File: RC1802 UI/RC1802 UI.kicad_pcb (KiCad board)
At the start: 2 copper layers, 99.1 x 80 mm, 44 parts, among them J1 Mount, J2 Mount, J3 Mount, J4 Mount, J6 CONN_02X20, SW1 CLEAR, SW10 IN5, SW11 IN6, SW12 IN7, SW2 IN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

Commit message: Tied leftover LS04 and 4050 inputs low
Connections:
- U1 pad 13: (no net) -> GND
- U2 pad 11: (no net) -> GND
- U2 pad 14: (no net) -> GND
- U2 pad 7: (no net) -> GND
- U2 pad 9: (no net) -> GND
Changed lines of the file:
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@@
 (kicad_pcb (version 4) (host pcbnew 4.0.7)
   (general
-    (links 160)
+    (links 165)
     (no_connects 0)
     (area 100.254999 67.234999 199.465001 147.395001)
@@
     (pad 1 thru_hole rect (at 0 0) (size 1.6 1.6) (drill 0.8) (layers *.Cu *.Mask)
       (net 16 VCC))
-    (pad 9 thru_hole oval (at 7.62 17.78) (size 1.6 1.6) (drill 0.8) (layers *.Cu *.Mask))
+    (pad 9 thru_hole oval (at 7.62 17.78) (size 1.6 1.6) (drill 0.8) (layers *.Cu *.Mask)
+      (net 3 GND))
     (pad 2 thru_hole oval (at 0 2.54) (size 1.6 1.6) (drill 0.8) (layers *.Cu *.Mask)
       (net 60 ~CLEAR))
@@
     (pad 3 thru_hole oval (at 0 5.08) (size 1.6 1.6) (drill 0.8) (layers *.Cu *.Mask)
       (net 60 ~CLEAR))
-    (pad 11 thru_hole oval (at 7.62 12.7) (size 1.6 1.6) (drill 0.8) (layers *.Cu *.Mask))
+    (pad 11 thru_hole oval (at 7.62 12.7) (size 1.6 1.6) (drill 0.8) (layers *.Cu *.Mask)
+      (net 3 GND))
     (pad 4 thru_hole oval (at 0 7.62) (size 1.6 1.6) (drill 0.8) (layers *.Cu *.Mask)
       (net 48 STROBE))
@@
     (pad 13 thru_hole oval (at 7.62 7.62) (size 1.6 1.6) (drill 0.8) (layers *.Cu *.Mask))
     (pad 6 thru_hole oval (at 0 12.7) (size 1.6 1.6) (drill 0.8) (layers *.Cu *.Mask))
-    (pad 14 thru_hole oval (at 7.62 5.08) (size 1.6 1.6) (drill 0.8) (layers *.Cu *.Mask))
-    (pad 7 thru_hole oval (at 0 15.24) (size 1.6 1.6) (drill 0.8) (layers *.Cu *.Mask))
+    (pad 14 thru_hole oval (at 7.62 5.08) (size 1.6 1.6) (drill 0.8) (layers *.Cu *.Mask)
+      (net 3 GND))
+    (pad 7 thru_hole oval (at 0 15.24) (size 1.6 1.6) (drill 0.8) (layers *.Cu *.Mask)
+      (net 3 GND))
     (pad 15 thru_hole oval (at 7.62 2.54) (size 1.6 1.6) (drill 0.8) (layers *.Cu *.Mask))
     (pad 8 thru_hole oval (at 0 17.78) (size 1.6 1.6) (drill 0.8) (layers *.Cu *.Mask)
@@
     (pad 6 thru_hole oval (at 0 12.7) (size 1.6 1.6) (drill 0.8) (layers *.Cu *.Mask)
       (net 59 ~WAIT))
-    (pad 13 thru_hole oval (at 7.62 2.54) (size 1.6 1.6) (drill 0.8) (layers *.Cu *.Mask))
+    (pad 13 thru_hole oval (at 7.62 2.54) (size 1.6 1.6) (drill 0.8) (layers *.Cu *.Mask)
+      (net 3 GND))
     (pad 7 thru_hole oval (at 0 15.24) (size 1.6 1.6) (drill 0.8) (layers *.Cu *.Mask)
       (net 3 GND))

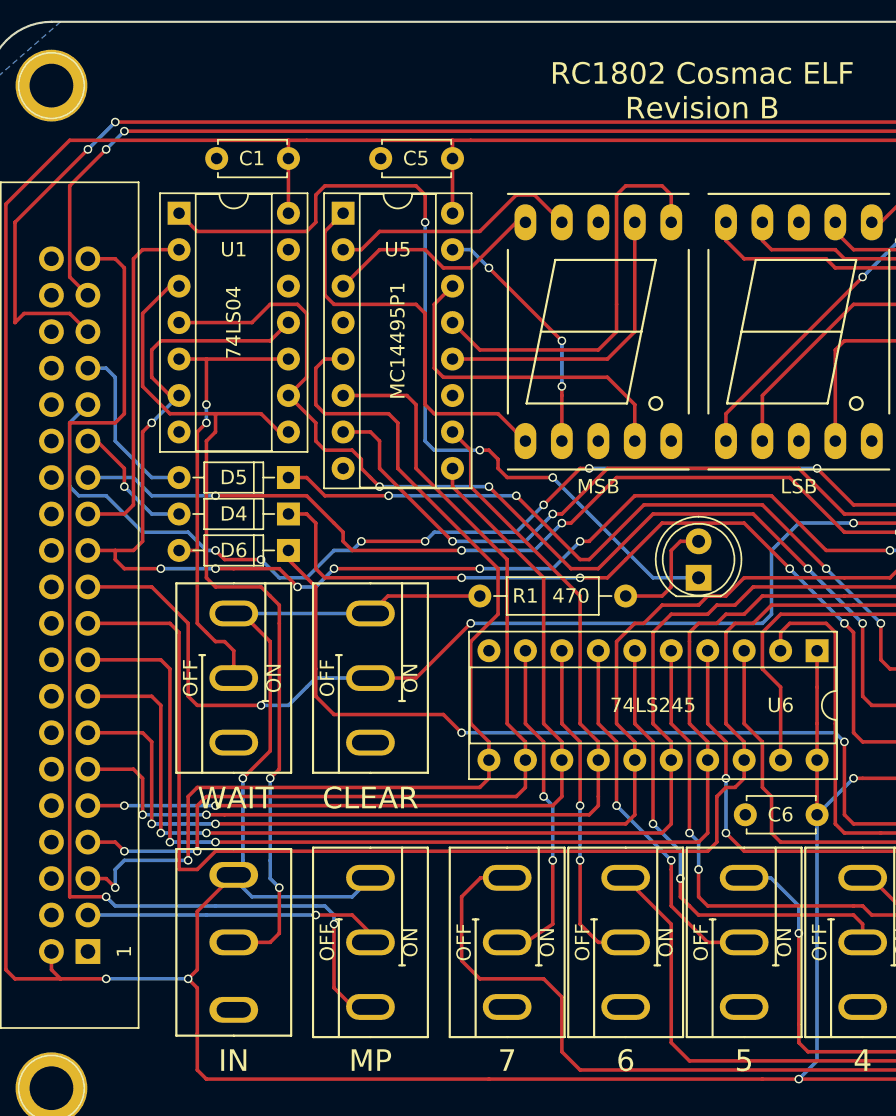
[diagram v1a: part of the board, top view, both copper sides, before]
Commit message: Fixed issue with in button, seems I should have read missing datasheet!
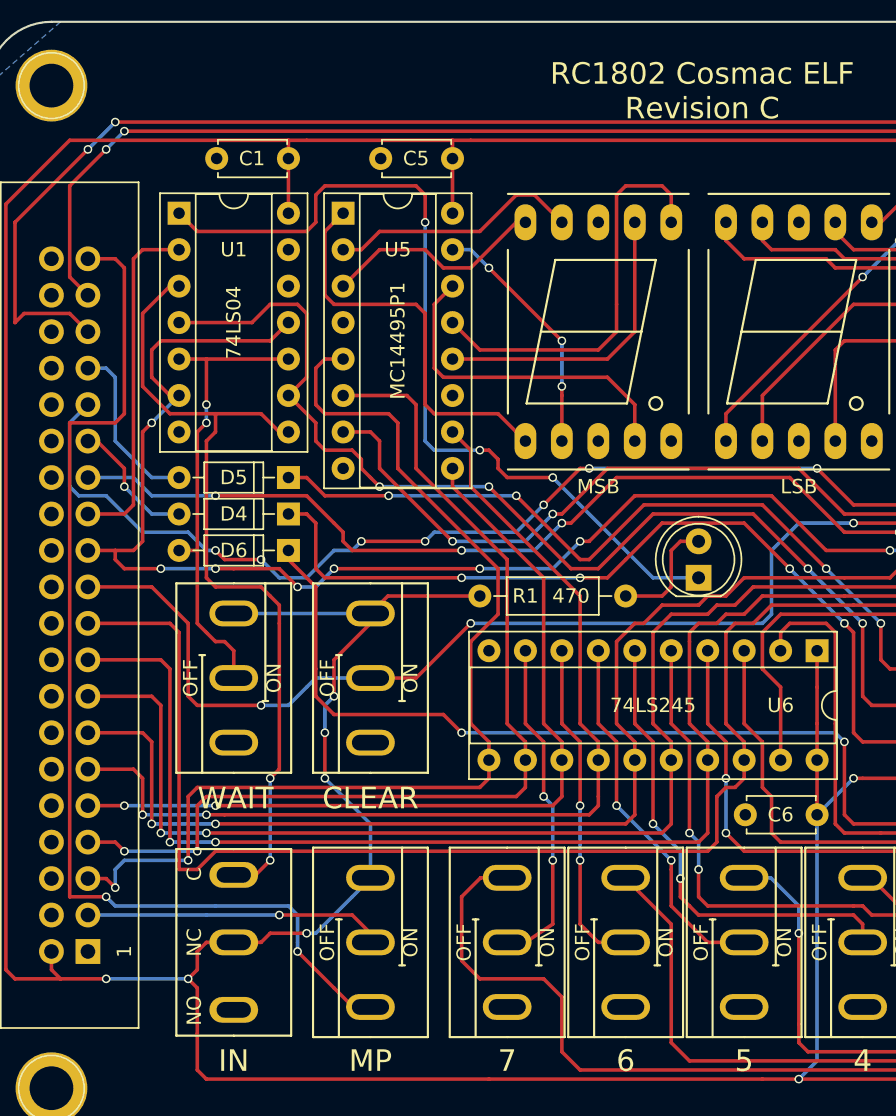
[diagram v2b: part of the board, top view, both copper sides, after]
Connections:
- SW2 pad 1: GND -> Net-(SW2-Pad1)
- SW2 pad 2: Net-(SW2-Pad2) -> VCC
- SW2 pad 3: VCC -> GND
- U1 pad 3: Net-(SW2-Pad2) -> Net-(SW2-Pad1)
- U1 pad 8: Net-(SW2-Pad2) -> Net-(SW2-Pad1)
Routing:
- net Net-(SW2-Pad2): track 64.3 -> 0.00 mm, vias 2 -> 0
- net Net-(SW2-Pad1): track 0.00 -> 58.4 mm, vias 0 -> 2
- net MWR: track 77.2 -> 75.7 mm
- net VCC: track 371.4 -> 370.5 mm, vias 5 -> 8
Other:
- board text added: "RC1802 Cosmac ELF Revision C"
- board text removed: "RC1802 Cosmac ELF Revision B"

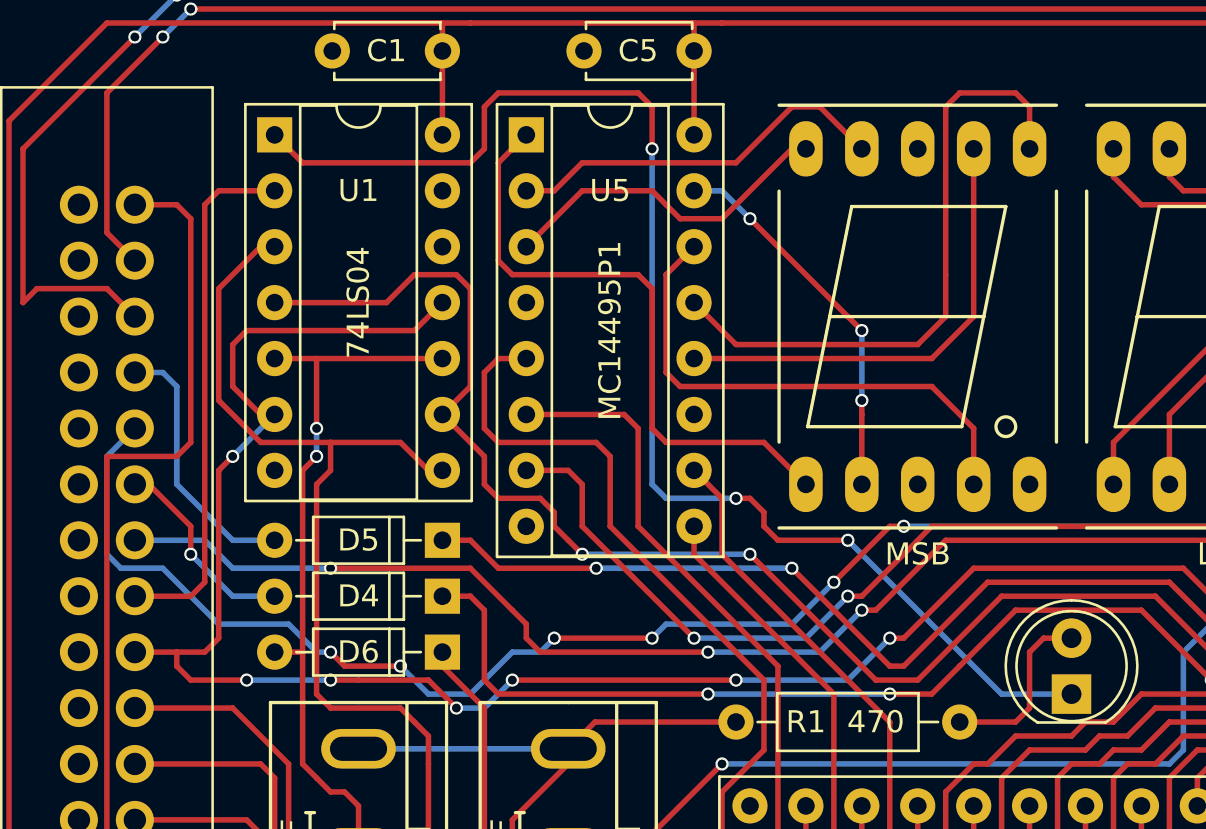
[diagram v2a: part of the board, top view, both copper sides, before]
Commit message: Q signal inverter wrong way around!
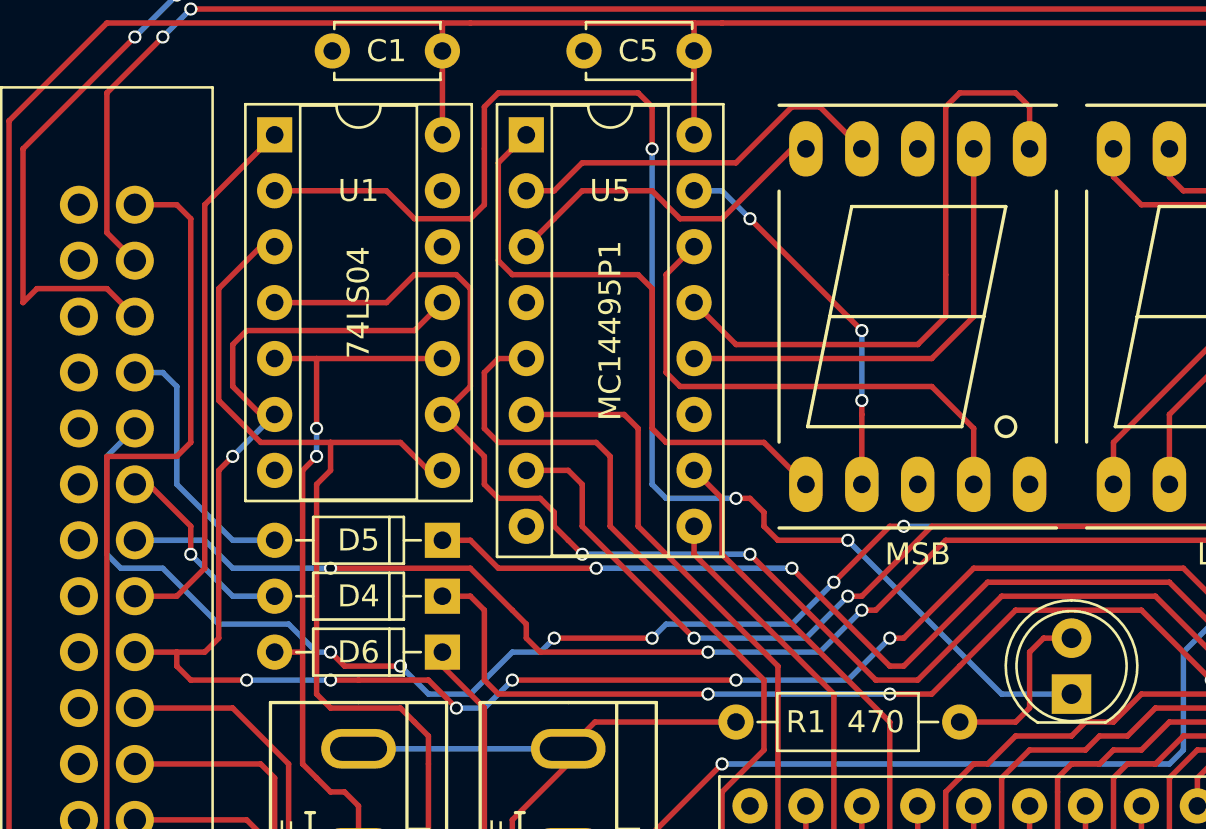
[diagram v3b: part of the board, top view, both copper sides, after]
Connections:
- U1 pad 1: Net-(D1-Pad1) -> Q
- U1 pad 2: Q -> Net-(D1-Pad1)
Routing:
- net Net-(D1-Pad1): track 60.9 -> 63.4 mm
- net Q: track 24.7 -> 25.3 mm
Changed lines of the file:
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@@
     (thickness 1.6)
     (drawings 29)
-    (tracks 1084)
+    (tracks 1085)
     (zones 0)
     (modules 44)
@@
     )
     (pad 1 thru_hole rect (at 0 0) (size 1.6 1.6) (drill 0.8) (layers *.Cu *.Mask)
-      (net 17 "Net-(D1-Pad1)"))
+      (net 28 Q))
     (pad 8 thru_hole oval (at 7.62 15.24) (size 1.6 1.6) (drill 0.8) (layers *.Cu *.Mask)
       (net 63 "Net-(SW2-Pad1)"))
     (pad 2 thru_hole oval (at 0 2.54) (size 1.6 1.6) (drill 0.8) (layers *.Cu *.Mask)
-      (net 28 Q))
+      (net 17 "Net-(D1-Pad1)"))
     (pad 9 thru_hole oval (at 7.62 12.7) (size 1.6 1.6) (drill 0.8) (layers *.Cu *.Mask)
       (net 18 /~IN))
@@
   (segment (start 104.775 133.35) (end 105.41 133.985) (width 0.25) (layer F.Cu) (net 16))
   (segment (start 158.115 118.745) (end 158.115 122.555) (width 0.25) (layer F.Cu) (net 16))
-  (segment (start 113.665 80.645) (end 114.935 81.915) (width 0.25) (layer F.Cu) (net 17))
+  (segment (start 123.19 81.28) (end 123.19 83.82) (width 0.25) (layer F.Cu) (net 17))
+  (segment (start 123.19 81.28) (end 123.19 79.375) (width 0.25) (layer F.Cu) (net 17))
+  (segment (start 123.19 79.375) (end 123.825 78.74) (width 0.25) (layer F.Cu) (net 17))
+  (segment (start 123.825 78.74) (end 130.175 78.74) (width 0.25) (layer F.Cu) (net 17))
+  (segment (start 130.175 78.74) (end 130.81 79.375) (width 0.25) (layer F.Cu) (net 17))
+  (segment (start 130.81 79.375) (end 130.81 81.28) (width 0.25) (layer F.Cu) (net 17))
+  (via (at 130.81 81.28) (size 0.6) (drill 0.4) (layers F.Cu B.Cu) (net 17))
+  (segment (start 130.81 81.28) (end 130.81 96.52) (width 0.25) (layer B.Cu) (net 17))
+  (segment (start 130.81 96.52) (end 131.445 97.155) (width 0.25) (layer B.Cu) (net 17))
+  (segment (start 131.445 97.155) (end 134.62 97.155) (width 0.25) (layer B.Cu) (net 17))
+  (via (at 134.62 97.155) (size 0.6) (drill 0.4) (layers F.Cu B.Cu) (net 17))
+  (segment (start 134.62 97.155) (end 135.255 97.155) (width 0.25) (layer F.Cu) (net 17))
+  (segment (start 135.255 97.155) (end 135.89 97.79) (width 0.25) (layer F.Cu) (net 17))
+  (segment (start 135.89 97.79) (end 135.89 98.425) (width 0.25) (layer F.Cu) (net 17))
+  (segment (start 149.86 106.045) (end 146.685 106.045) (width 0.25) (layer B.Cu) (net 17))
+  (segment (start 136.525 99.06) (end 135.89 98.425) (width 0.25) (layer F.Cu) (net 17))
+  (segment (start 139.7 99.06) (end 136.525 99.06) (width 0.25) (layer F.Cu) (net 17))
+  (via (at 139.7 99.06) (size 0.6) (drill 0.4) (layers F.Cu B.Cu) (net 17))
   (segment (start 146.685 106.045) (end 139.7 99.06) (width 0.25) (layer B.Cu) (net 17))
-  (via (at 139.7 99.06) (size 0.6) (drill 0.4) (layers F.Cu B.Cu) (net 17))
-  (segment (start 139.7 99.06) (end 136.525 99.06) (width 0.25) (layer F.Cu) (net 17))
-  (segment (start 136.525 99.06) (end 135.89 98.425) (width 0.25) (layer F.Cu) (net 17))
-  (segment (start 146.685 106.045) (end 149.86 106.045) (width 0.25) (layer B.Cu) (net 17))
-  (segment (start 135.89 97.79) (end 135.89 98.425) (width 0.25) (layer F.Cu) (net 17))
-  (segment (start 135.255 97.155) (end 135.89 97.79) (width 0.25) (layer F.Cu) (net 17))
-  (segment (start 134.62 97.155) (end 135.255 97.155) (width 0.25) (layer F.Cu) (net 17))
-  (via (at 134.62 97.155) (size 0.6) (drill 0.4) (layers F.Cu B.Cu) (net 17))
-  (segment (start 131.445 97.155) (end 134.62 97.155) (width 0.25) (layer B.Cu) (net 17))
-  (segment (start 130.81 96.52) (end 131.445 97.155) (width 0.25) (layer B.Cu) (net 17))
-  (segment (start 130.81 81.28) (end 130.81 96.52) (width 0.25) (layer B.Cu) (net 17))
-  (via (at 130.81 81.28) (size 0.6) (drill 0.4) (layers F.Cu B.Cu) (net 17))
-  (segment (start 130.81 79.375) (end 130.81 81.28) (width 0.25) (layer F.Cu) (net 17))
-  (segment (start 130.175 78.74) (end 130.81 79.375) (width 0.25) (layer F.Cu) (net 17))
-  (segment (start 123.825 78.74) (end 130.175 78.74) (width 0.25) (layer F.Cu) (net 17))
-  (segment (start 123.19 79.375) (end 123.825 78.74) (width 0.25) (layer F.Cu) (net 17))
-  (segment (start 123.19 81.28) (end 123.19 79.375) (width 0.25) (layer F.Cu) (net 17))
-  (segment (start 122.555 81.915) (end 123.19 81.28) (width 0.25) (layer F.Cu) (net 17))
-  (segment (start 114.935 81.915) (end 122.555 81.915) (width 0.25) (layer F.Cu) (net 17))
+  (segment (start 118.745 83.185) (end 113.665 83.185) (width 0.25) (layer F.Cu) (net 17))
+  (segment (start 120.015 84.455) (end 118.745 83.185) (width 0.25) (layer F.Cu) (net 17))
+  (segment (start 122.555 84.455) (end 120.015 84.455) (width 0.25) (layer F.Cu) (net 17))
+  (segment (start 123.19 83.82) (end 122.555 84.455) (width 0.25) (layer F.Cu) (net 17))
   (segment (start 177.8 116.84) (end 179.705 116.84) (width 0.25) (layer B.Cu) (net 18))
   (via (at 186.055 116.84) (size 0.6) (drill 0.4) (layers F.Cu B.Cu) (net 18))
@@
   (segment (start 187.96 93.98) (end 187.325 94.615) (width 0.25) (layer F.Cu) (net 27))
   (segment (start 187.96 92.075) (end 187.96 93.98) (width 0.25) (layer F.Cu) (net 27))
+  (segment (start 107.315 101.6) (end 109.22 101.6) (width 0.25) (layer F.Cu) (net 28))
+  (segment (start 110.49 83.82) (end 113.665 80.645) (width 0.25) (layer F.Cu) (net 28))
+  (segment (start 110.49 100.33) (end 110.49 83.82) (width 0.25) (layer F.Cu) (net 28))
+  (segment (start 109.22 101.6) (end 110.49 100.33) (width 0.25) (layer F.Cu) (net 28))
   (segment (start 107.95 101.6) (end 107.315 101.6) (width 0.25) (layer B.Cu) (net 28))
-  (segment (start 107.315 101.6) (end 109.855 101.6) (width 0.25) (layer F.Cu) (net 28))
-  (segment (start 111.125 83.185) (end 113.665 83.185) (width 0.25) (layer F.Cu) (net 28))
-  (segment (start 110.49 83.82) (end 111.125 83.185) (width 0.25) (layer F.Cu) (net 28))
-  (segment (start 110.49 100.965) (end 110.49 83.82) (width 0.25) (layer F.Cu) (net 28))
-  (segment (start 109.855 101.6) (end 110.49 100.965) (width 0.25) (layer F.Cu) (net 28))
   (segment (start 121.92 131.445) (end 121.92 132.08) (width 0.25) (layer B.Cu) (net 29))
   (segment (start 124.46 134.62) (end 121.92 132.08) (width 0.25) (layer F.Cu) (net 29))

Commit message: Regenerate netlist
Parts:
- removed RN1: 100k, Resistors_THT:R_Array_SIP9
- added JP1: DP_READ, Pin_Headers:Pin_Header_Straight_1x02_Pitch2.54mm, F.Cu at (144.1, 153.7)
- added JP2: DP_STROBE, Pin_Headers:Pin_Header_Straight_1x02_Pitch2.54mm, F.Cu at (151.1, 159.4)
- added R4: 330, Resistors_THT:R_Axial_DIN0207_L6.3mm_D2.5mm_P10.16mm_Horizontal, F.Cu at (156.2, 151.8)
- added R5: 330, Resistors_THT:R_Axial_DIN0207_L6.3mm_D2.5mm_P10.16mm_Horizontal, F.Cu at (160.0, 160.0)
- AFF1: value MSB -> MSD
- AFF2: value LSB -> LSD
- U6: value 74LS245 -> 74LS244
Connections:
- AFF1 pad 5: (no net) -> Net-(AFF1-Pad5)
- AFF2 pad 5: (no net) -> Net-(AFF2-Pad5)
- D1 pad 1: Net-(D1-Pad1) -> ~Q
- J6 pad 25: Q -> (no net)
- J6 pad 26: GND -> ~Q
- SW10 pad 3: Net-(RN1-Pad4) -> VCC
- SW11 pad 3: Net-(RN1-Pad3) -> VCC
- SW12 pad 3: Net-(RN1-Pad2) -> VCC
- SW5 pad 3: Net-(RN1-Pad9) -> VCC
- SW6 pad 3: Net-(RN1-Pad8) -> VCC
- SW7 pad 3: Net-(RN1-Pad7) -> VCC
- SW8 pad 3: Net-(RN1-Pad6) -> VCC
- SW9 pad 3: Net-(RN1-Pad5) -> VCC
- U1 pad 1: Q -> GND
- U1 pad 2: Net-(D1-Pad1) -> (no net)
- U2 pad 6: (no net) -> READ
- U2 pad 7: GND -> Net-(U2-Pad7)
- U4 pad 10: TPB -> LOAD_N2
- U4 pad 11: Net-(U4-Pad11) -> TPB
- U4 pad 12: Net-(U4-Pad11) -> Net-(U4-Pad12)
- U4 pad 6: READ -> Net-(U2-Pad7)
- U4 pad 9: LOAD_N2 -> Net-(U4-Pad12)
- U5 pad 10: /BUS4 -> /BUS7
- U5 pad 5: /BUS7 -> /BUS4
- U5 pad 6: /BUS6 -> /BUS5
- U5 pad 9: /BUS5 -> /BUS6
- U6 pad 1: VCC -> READ
- U6 pad 11: /BUS7 -> Net-(SW9-Pad2)
- U6 pad 12: /BUS6 -> /BUS3
- U6 pad 13: /BUS5 -> Net-(SW10-Pad2)
- U6 pad 14: /BUS4 -> /BUS2
- U6 pad 15: /BUS3 -> Net-(SW11-Pad2)
- U6 pad 16: /BUS2 -> /BUS1
- U6 pad 17: /BUS1 -> Net-(SW12-Pad2)
- U6 pad 3: Net-(SW6-Pad2) -> /BUS7
- U6 pad 4: Net-(SW7-Pad2) -> Net-(SW6-Pad2)
- U6 pad 5: Net-(SW8-Pad2) -> /BUS6
- U6 pad 6: Net-(SW9-Pad2) -> Net-(SW7-Pad2)
- U6 pad 7: Net-(SW10-Pad2) -> /BUS5
- U6 pad 8: Net-(SW11-Pad2) -> Net-(SW8-Pad2)
- U6 pad 9: Net-(SW12-Pad2) -> /BUS4
- U7 pad 10: /BUS0 -> /BUS3
- U7 pad 5: /BUS3 -> /BUS0
- U7 pad 6: /BUS2 -> /BUS1
- U7 pad 9: /BUS1 -> /BUS2
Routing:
- net /BUS2: track 106.8 -> 0.00 mm, vias 2 -> 0
- net TPB: track 105.6 -> 0.00 mm, vias 11 -> 0
- net /BUS3: track 103.5 -> 0.00 mm, vias 4 -> 0
- net /BUS7: track 74.6 -> 0.00 mm, vias 2 -> 0
- net /BUS6: track 69.6 -> 0.00 mm, vias 2 -> 0
- net /BUS4: track 68.9 -> 0.00 mm, vias 2 -> 0
- net ~Q: track 0.00 -> 63.4 mm, vias 0 -> 3
- net Net-(D1-Pad1): track 63.4 -> 0.00 mm, vias 3 -> 0
- net /BUS5: track 59.3 -> 0.00 mm, vias 2 -> 0
- net MWR: track 75.7 -> 19.5 mm, vias 2 -> 0
- net Net-(RN1-Pad2): track 53.9 -> 0.00 mm
- net /BUS1: track 103.4 -> 52.3 mm, vias 2 -> 0
- net Net-(SW6-Pad2): track 50.0 -> 0.00 mm
- net READ: track 48.9 -> 0.00 mm
- net /BUS0: track 112.9 -> 68.3 mm
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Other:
- board text removed: "MP"
